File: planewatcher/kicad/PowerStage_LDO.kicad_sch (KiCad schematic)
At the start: 11 parts, among them U6 LT3045IMSE-1#PBF

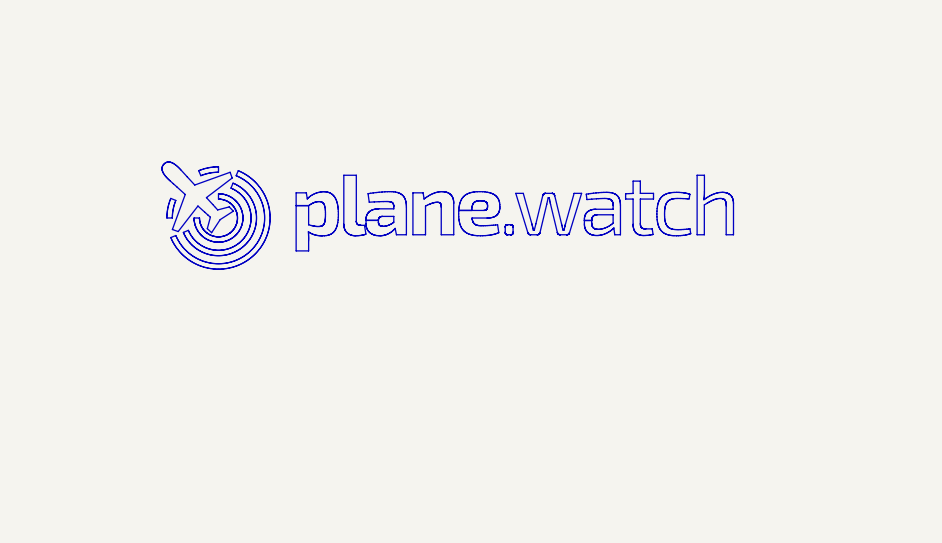
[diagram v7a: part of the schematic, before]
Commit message: add license & copyright info to schematic and pcb. fix layer window.
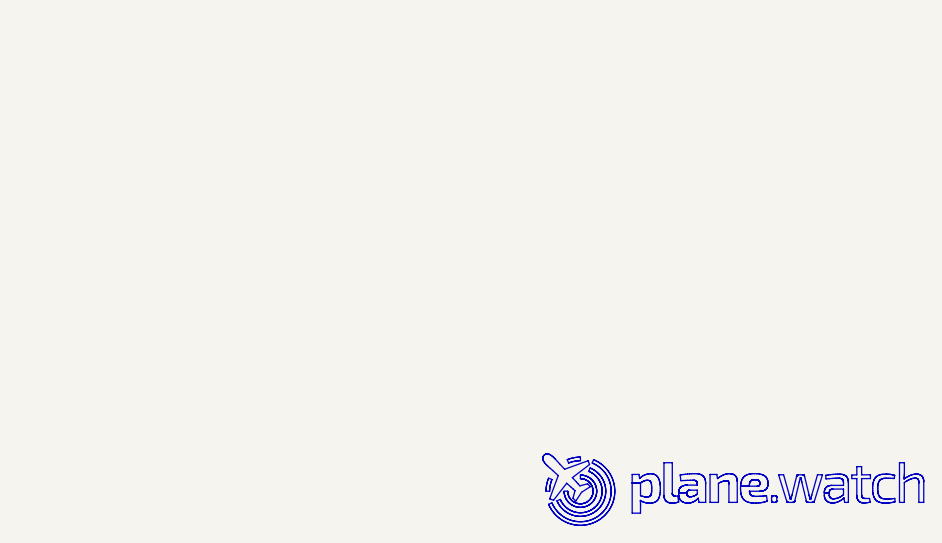
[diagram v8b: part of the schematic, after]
